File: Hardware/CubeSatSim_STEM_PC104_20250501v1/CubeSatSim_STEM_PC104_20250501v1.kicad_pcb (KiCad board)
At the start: 2 copper layers, 90.2 x 95.9 mm, 211 parts, among them J1 Conn_02x20_Odd_Even, J2 Conn_01x04, J23 Conn_01x04, J4 Conn_01x04, U2 Pico, U3 MPU6050, U4 BME280

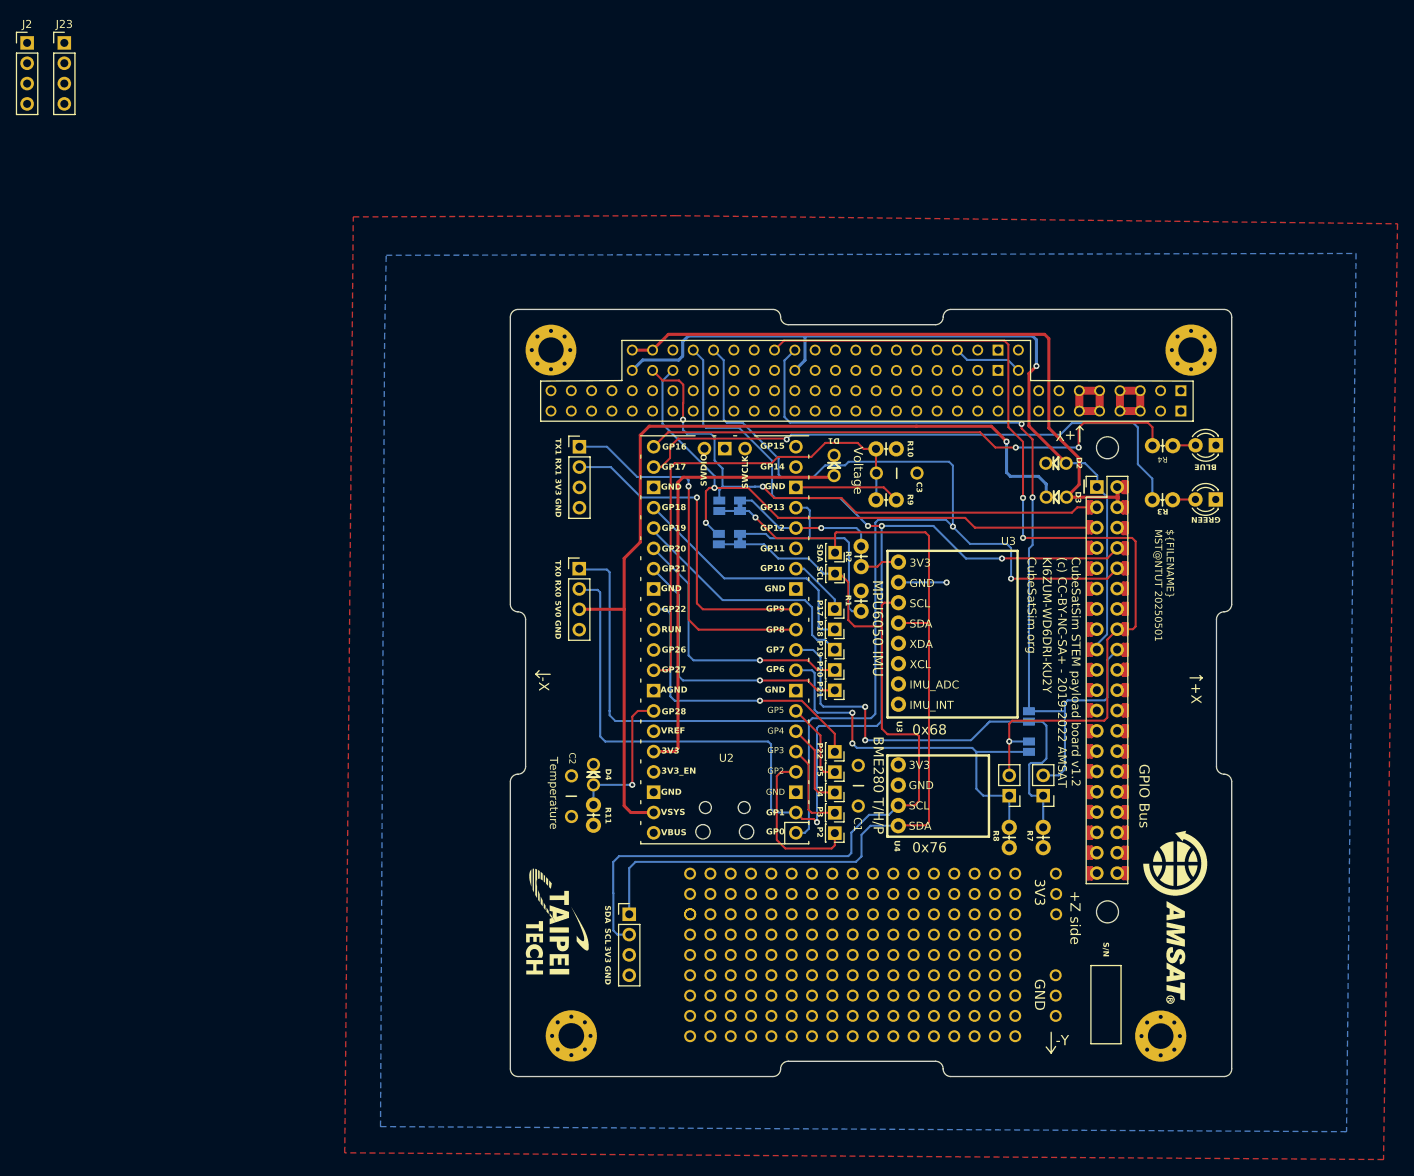
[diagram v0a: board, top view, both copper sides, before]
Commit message: 1. Swap I2C connector and temperature sensor on STEM board. 2. Add  marks  on side  connectors. 3. Copy FlatSat project to new project dated 20250506. Update date on flatsat board.
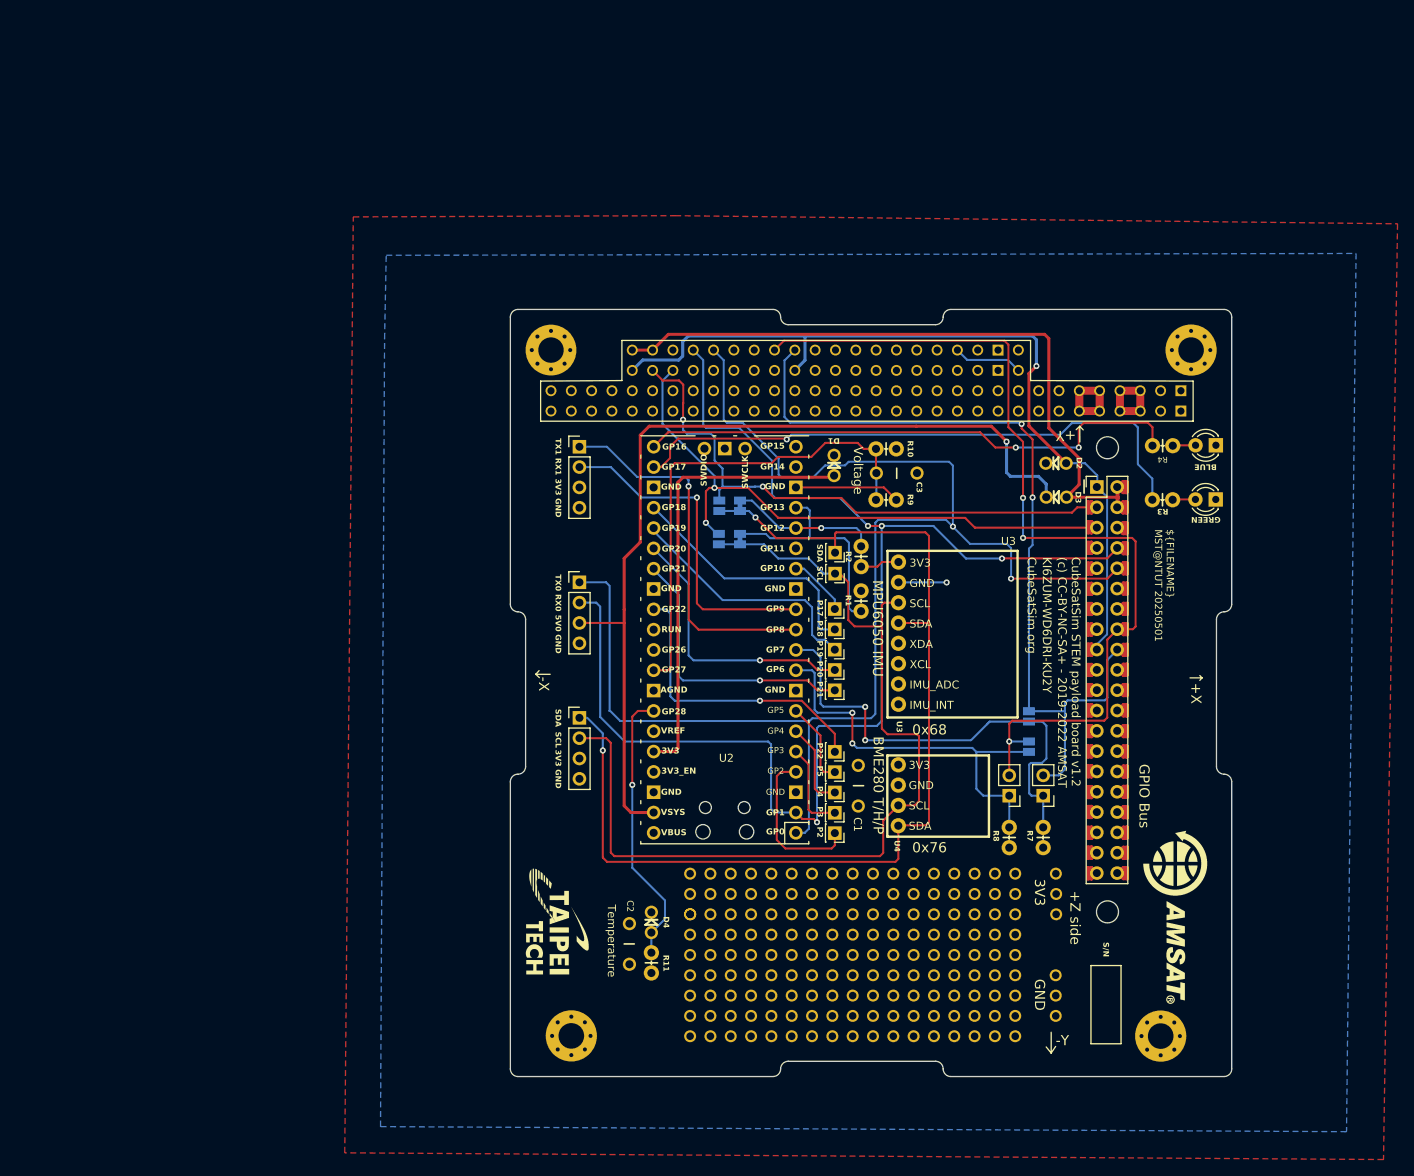
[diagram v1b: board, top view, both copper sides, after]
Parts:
- removed the J2 at (1.82, 1.82)
- removed the J23 at (6.47, 1.82)
- moved J2 25.3 mm to (70.9, 86.2)
- moved C2 19.8 mm to (77.1, 114.5)
- moved D4 19.8 mm to (79.9, 111.8)
- moved R11 19.8 mm to (79.9, 116.8)
- moved J4 1.70 mm to (70.9, 69.2)
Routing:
- net /SDA: track 117.0 -> 134.6 mm, vias 1 -> 2
- net /TEMPERATURE: track 18.9 -> 34.9 mm
- net /SCL: track 112.3 -> 120.5 mm
- net /PI_TXD: track 178.3 -> 175.2 mm
- net /PI_RXD: track 186.7 -> 184.7 mm
